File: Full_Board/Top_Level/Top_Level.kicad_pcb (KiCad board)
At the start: 2 copper layers, 160 parts, among them IC1 DRV8824QPWPRQ1, IC2 DRV8824QPWPRQ1, IC3 DRV8824QPWPRQ1, J1 OQ0432500000G, J1-J1 Conn_01x10, J1/J3 SSQ-110-03-T-D, J10 TSW-149-07-S-D, J101 PEC10DAAN, J108 TC2050-IDC-NL-FP, J12 PEC03SAAN, J13 PEC03SAAN, J2 OQ0432500000G, J2/J4 SSQ-110-03-T-D, J3 OQ0432500000G, J4 OQ0212500000G, J4-J1 Conn_01x10, J5 OQ0212500000G, J5-J1 Conn_01x10, J5/J7 SSQ-110-03-T-D, J6 KLDHCX-8-0202-A, J6/J8 SSQ-110-03-T-D, J7 OQ0212500000G, J8-J1 Conn_01x10, U1 LM2576SX-3.3-NOPB, U14 1-406541-1, U7 ZX62D-AB-5P8

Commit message: Fix MSP connector spacing
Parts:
- removed BSL: AWHW-10G-0202-T, Connectors_Other.IntLib:Assman_AWHW-10G-0x02-T
- removed CE Logo: CE Mark, Logos.IntLib:CE_Mark_5mm
- removed J1-J1, J4-J1, J5-J1, J8-J1: Conn_01x10, Connector_PinSocket_2.54mm:PinSocket_2x10_P2.54mm_Vertical
- removed J1/J3, J5/J7: SSQ-110-03-T-D, Hardware.IntLib:BoosterPack_40pin_J1J3
- removed J10: TSW-149-07-S-D, Connectors_Samtec1.IntLib:Samtec_TSW-149-07-x-D
- removed J101: PEC10DAAN, Connectors_Sullins.IntLib:SULLINS_PEC10DAAN
- removed J108: TC2050-IDC-NL-FP, Connectors_Other.IntLib:Tag_TC2050-NL
- removed J12: PEC03SAAN, Connectors_Sullins.IntLib:PEC03SAAN_Launchpad_3V3
- removed J13: PEC03SAAN, Connectors_Sullins.IntLib:PEC03SAAN_Launchpad_5V0
- removed J2/J4, J6/J8: SSQ-110-03-T-D, Hardware.IntLib:BoosterPack_40pin_J2J4
- removed JP1: PEC03DAAN, Connectors_Sullins.IntLib:SULLINS_PEC03DAAN
- removed JP2, JP6, JP7: PEC02SAAN, Connectors_Sullins.IntLib:CONN_PEC02SAAN
- removed JP4, JP5: PBC02DAAN, Connectors_Sullins.IntLib:Sullins_PxC02DAAN
- removed Logo1: Texas Instruments, Logos.IntLib:TI_Stacked_Overlay_Small
- removed MH1, MH2: MTG_NoPads, Hardware.IntLib:NPTH125mil
- removed RESET_SW1, USR_SW1, USR_SW2, Wake_SW4: 1188E-1K2-V-TR, Switches.IntLib:SW_1188E
- removed TI Logo: Texas Instruments, Logos.IntLib:TI_Symbol_Overlay_Medium
- removed TI Logo 2: Texas Instruments, Logos.IntLib:TI_Horizontal_Overlay_Small
- removed the TP10 at (356.9, 160.0)
- removed the TP10 at (62.5, 174.0)
- removed the TP11 at (83.2, 155.5)
- removed the TP11 at (367.0, 157.5)
- removed the TP12 at (367.0, 127.0)
- removed the TP12 at (76.6, 160.5)
- removed the TP13 at (65.1, 169.0)
- removed the TP13 at (356.9, 127.0)
- removed the TP14 at (78.2, 155.5)
- removed the TP14 at (384.8, 167.6)
- removed the TP15 at (117.0, 138.8)
- removed the TP15 at (336.6, 106.7)
- removed the TP16 at (361.9, 94.0)
- removed the TP16 at (116.4, 143.9)
- removed the TP17 at (372.1, 108.0)
- removed the TP17 at (108.8, 148.1)
- removed the TP4 at (75.2, 120.7)
- removed the TP4 at (364.5, 177.8)
- removed the TP5 at (68.6, 125.7)
- removed the TP5 at (367.0, 177.8)
- removed the TP6 at (57.1, 134.2)
- removed the TP6 at (369.6, 177.8)
- removed the TP7 at (372.1, 177.8)
- removed the TP7 at (70.2, 120.7)
- removed the TP8 at (351.8, 106.7)
- removed the TP8 at (70.7, 164.7)
- removed the TP9 at (359.4, 160.0)
- removed the TP9 at (70.1, 169.8)
- removed U14: 1-406541-1, Connectors_TE_Connectivity.IntLib:TEC_1-406541-1
- removed U7: ZX62D-AB-5P8, Connectors_Other.IntLib:Hirose-ZX62D-AB-5P8
- removed USB101: 1051640001, Connectors_Molex.IntLib:Molex_1051640001
- added D8: TPD1E10B06DPYR, TPD1E10B06DPYR:TPD1E10B06DPYR, F.Cu at (241.5, 70.6)
- added D9: TPD1E10B06DPYR, TPD1E10B06DPYR:TPD1E10B06DPYR, F.Cu at (242.3, 43.8)
- added J1-J3: Conn_01x10, Connector_PinSocket_2.54mm:PinSocket_2x10_P2.54mm_Vertical, F.Cu at (26.7, 21.6)
- added J4-J2: Conn_01x10, Connector_PinSocket_2.54mm:PinSocket_2x10_P2.54mm_Vertical, F.Cu at (69.9, 21.6)
- added J5-J7: Conn_01x10, Connector_PinSocket_2.54mm:PinSocket_2x10_P2.54mm_Vertical, F.Cu at (26.7, 85.1)
- added J8: OQ0212500000G, OQ0212500000G:OQ0212500000G, F.Cu at (231.1, 47.9)
- added J8-J6: Conn_01x10, Connector_PinSocket_2.54mm:PinSocket_2x10_P2.54mm_Vertical, F.Cu at (69.9, 85.1)
- added R43: CR0402-FX-5620GLF, CR0402-FX-5620GLF:RESC1005X40N, F.Cu at (266.9, 42.0)
- added R44: CR0402-FX-5620GLF, CR0402-FX-5620GLF:RESC1005X40N, F.Cu at (262.4, 44.9)
- added TP10: TestPoint, TestPoint:TestPoint_Keystone_5010-5014_Multipurpose, F.Cu at (128.1, 109.9)
- added TP11: TestPoint, TestPoint:TestPoint_Keystone_5010-5014_Multipurpose, F.Cu at (148.8, 91.4)
- added TP12: TestPoint, TestPoint:TestPoint_Keystone_5010-5014_Multipurpose, F.Cu at (142.2, 96.4)
- added TP13: TestPoint, TestPoint:TestPoint_Keystone_5010-5014_Multipurpose, F.Cu at (130.7, 104.9)
- added TP14: TestPoint, TestPoint:TestPoint_Keystone_5010-5014_Multipurpose, F.Cu at (143.8, 91.4)
- added TP15: TestPoint, TestPoint:TestPoint_Keystone_5010-5014_Multipurpose, F.Cu at (199.6, 29.0)
- added TP16: TestPoint, TestPoint:TestPoint_Keystone_5010-5014_Multipurpose, F.Cu at (199.1, 34.0)
- added TP17: TestPoint, TestPoint:TestPoint_Keystone_5010-5014_Multipurpose, F.Cu at (191.4, 38.3)
- added TP4: TestPoint, TestPoint:TestPoint_Keystone_5010-5014_Multipurpose, F.Cu at (196.7, 56.6)
- added TP5: TestPoint, TestPoint:TestPoint_Keystone_5010-5014_Multipurpose, F.Cu at (190.0, 61.7)
- added TP6: TestPoint, TestPoint:TestPoint_Keystone_5010-5014_Multipurpose, F.Cu at (178.5, 70.2)
- added TP7: TestPoint, TestPoint:TestPoint_Keystone_5010-5014_Multipurpose, F.Cu at (191.6, 56.6)
- added TP8: TestPoint, TestPoint:TestPoint_Keystone_5010-5014_Multipurpose, F.Cu at (136.3, 100.6)
- added TP9: TestPoint, TestPoint:TestPoint_Keystone_5010-5014_Multipurpose, F.Cu at (135.7, 105.7)
- D5: value 31DQ04 -> TPD1E10B06DPYR; footprint Diode_THT:D_DO-201AD_P15.24mm_Horizontal -> TPD1E10B06DPYR:TPD1E10B06DPYR
- D7: value TPD1E10B06DPYR -> 31DQ04; footprint TPD1E10B06DPYR:TPD1E10B06DPYR -> Diode_THT:D_DO-201AD_P15.24mm_Horizontal
- J4: value OQ0212500000G -> OQ0432500000G; footprint OQ0212500000G:OQ0212500000G -> OQ0432500000G:RHDR4W80P0X381_1X4_1540X700X920P
- J6: value KLDHCX-8-0202-A -> OQ0212500000G; footprint KLDHCX-8-0202-A:KLDHCX80202A -> OQ0212500000G:OQ0212500000G
- J7: value OQ0212500000G -> KLDHCX-8-0202-A; footprint OQ0212500000G:OQ0212500000G -> KLDHCX-8-0202-A:KLDHCX80202A
- R15: value CR0402-FX-5620GLF -> 2.2 k; footprint CR0402-FX-5620GLF:RESC1005X40N -> Resistor_THT:R_Axial_DIN0207_L6.3mm_D2.5mm_P10.16mm_Horizontal
- R16: value CRMA1210AF10K0DKEF -> 2.2 k; footprint CRMA1210AF10K0DKEF:RESC3225X74N -> Resistor_THT:R_Axial_DIN0207_L6.3mm_D2.5mm_P10.16mm_Horizontal
- R17, R20, R23, R26, R36, R39: value RCV2512100KFKEGAT -> CR0402-FX-5620GLF; footprint RCV2512100KFKEGAT:RESC6332X70N -> CR0402-FX-5620GLF:RESC1005X40N
- R18, R21, R24, R34, R37: value CR0402-FX-5620GLF -> CRMA1210AF10K0DKEF; footprint CR0402-FX-5620GLF:RESC1005X40N -> CRMA1210AF10K0DKEF:RESC3225X74N
- R19, R22, R25, R28, R38: value CRMA1210AF10K0DKEF -> RCV2512100KFKEGAT; footprint CRMA1210AF10K0DKEF:RESC3225X74N -> RCV2512100KFKEGAT:RESC6332X70N
- R27: value TNPV08051M00BEEA -> CRMA1210AF10K0DKEF; footprint TNPV08051M00BEEA:TNPV0805180KBEEA -> CRMA1210AF10K0DKEF:RESC3225X74N
- R29: value WSL2010R4000FEA -> TNPV08051M00BEEA; footprint WSL2010R4000FEA:RESC5025X88N -> TNPV08051M00BEEA:TNPV0805180KBEEA
- R30: value WSL2010R4000FEA -> CRMA1210AF10K0DKEF; footprint WSL2010R4000FEA:RESC5025X88N -> CRMA1210AF10K0DKEF:RESC3225X74N
- R31: value ERJ-PB6B3002V -> WSL2010R4000FEA; footprint ERJ-PB6B3002V:RESC2012X70N -> WSL2010R4000FEA:RESC5025X88N
- R32: value CRMA1210AF10K0DKEF -> WSL2010R4000FEA; footprint CRMA1210AF10K0DKEF:RESC3225X74N -> WSL2010R4000FEA:RESC5025X88N
- R33: value CRMA1210AF10K0DKEF -> ERJ-PB6B3002V; footprint CRMA1210AF10K0DKEF:RESC3225X74N -> ERJ-PB6B3002V:RESC2012X70N
- R40: value SDR10EZPJ271 -> CRMA1210AF10K0DKEF; footprint SDR10EZPJ271:RESC2012X65N -> CRMA1210AF10K0DKEF:RESC3225X74N
- R41: value CR0402-FX-5620GLF -> RCV2512100KFKEGAT; footprint CR0402-FX-5620GLF:RESC1005X40N -> RCV2512100KFKEGAT:RESC6332X70N
- R42: value CR0402-FX-5620GLF -> SDR10EZPJ271; footprint CR0402-FX-5620GLF:RESC1005X40N -> SDR10EZPJ271:RESC2012X65N
- moved D4 194.4 mm to (276.7, 19.0)
- moved J1 183.4 mm to (222.3, 22.2)
- moved J3 182.8 mm to (239.4, 30.7)
- moved R31 160.3 mm to (188.8, 19.1)
- moved C23 158.7 mm to (241.2, 47.7)
- moved R30 152.7 mm to (194.3, 28.6)
- moved TP3 152.0 mm to (176.0, 75.2)
- moved R39 151.3 mm to (237.6, 53.3)
- moved J7 150.2 mm to (161.2, 25.4)
- moved C4 145.3 mm to (184.9, 61.0)
- moved J2 143.5 mm to (239.4, 22.2)
- moved C2 143.1 mm to (173.3, 60.3)
- moved R1 143.0 mm to (179.5, 61.2)
- moved R3 142.9 mm to (173.3, 56.0)
- moved J4 141.3 mm to (222.3, 30.7)
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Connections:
- D1 pad 1: LS_Y_OUT -> /PiConnector1/Rx_MSP
- D2 pad 1: RESET_OUT -> /PiConnector1/Tx_MSP
- D3 pad 1: HOME_OUT -> LS_Y_OUT
- D4 pad 1: LS_Z_OUT -> RESET_OUT
- D5 pad 1: Net-(D5-Pad1) -> HOME_OUT
- D6 pad 1: START_OUT -> LS_Z_OUT
- D7 pad 1: LS_X_OUT -> Net-(D7-Pad1)
- J1 pad 1: /StepperDriver3/2B -> /PiConnector1/Rx_Pi
- J1 pad 2: /StepperDriver3/2A -> /PiConnector1/Tx_Pi
- J1 pad 3: /StepperDriver3/1B -> /PiConnector1/Tx_MSP
- J1 pad 4: /StepperDriver3/1A -> /PiConnector1/Rx_MSP
- J4 pad 1: GND -> /StepperDriver3/2B
- J4 pad 2: Net-(J4-Pad2) -> /StepperDriver3/2A
- J6 pad 2: +24V -> Net-(J6-Pad2)
- J7 pad 2: Net-(J7-Pad2) -> +24V
- L1 pad 2: Net-(D5-Pad1) -> Net-(D7-Pad1)
- R15 pad 1: Net-(J4-Pad2) -> /PiConnector1/Rx_MSP
- R15 pad 2: Net-(C11-Pad2) -> /PiConnector1/Tx_Pi
- R16 pad 1: Net-(C11-Pad2) -> /PiConnector1/Tx_MSP
- R16 pad 2: +3.3V -> /PiConnector1/Rx_Pi
- R17 pad 1: Net-(C11-Pad2) -> Net-(J5-Pad2)
- R17 pad 2: LS_Y_OUT -> Net-(C11-Pad2)
- R18 pad 1: Net-(R18-Pad1) -> Net-(C11-Pad2)
- R18 pad 2: Net-(C12-Pad2) -> +3.3V
- R19 pad 1: Net-(C12-Pad2) -> Net-(C11-Pad2)
- R19 pad 2: +3.3V -> LS_Y_OUT
- R20 pad 1: Net-(C12-Pad2) -> Net-(R20-Pad1)
- R20 pad 2: RESET_OUT -> Net-(C12-Pad2)
- R21 pad 1: Net-(R21-Pad1) -> Net-(C12-Pad2)
- R21 pad 2: Net-(C13-Pad2) -> +3.3V
- R22 pad 1: Net-(C13-Pad2) -> Net-(C12-Pad2)
- R22 pad 2: +3.3V -> RESET_OUT
- R23 pad 1: Net-(C13-Pad2) -> Net-(R23-Pad1)
- R23 pad 2: HOME_OUT -> Net-(C13-Pad2)
- R24 pad 1: Net-(J5-Pad2) -> Net-(C13-Pad2)
- R24 pad 2: Net-(C14-Pad2) -> +3.3V
- R25 pad 1: Net-(C14-Pad2) -> Net-(C13-Pad2)
- R25 pad 2: +3.3V -> HOME_OUT
- R26 pad 1: Net-(C14-Pad2) -> Net-(J6-Pad2)
- R26 pad 2: LS_Z_OUT -> Net-(C14-Pad2)
- R27 pad 1: +24V -> Net-(C14-Pad2)
- R27 pad 2: Net-(C18-Pad1) -> +3.3V
- R28 pad 1: GND -> Net-(C14-Pad2)
- R28 pad 2: Net-(IC3-Pad12) -> LS_Z_OUT
- R29 pad 1: GND -> +24V
- R29 pad 2: Net-(IC3-Pad6) -> Net-(C18-Pad1)
- R30 pad 2: Net-(IC3-Pad9) -> Net-(IC3-Pad12)
- R31 pad 1: Net-(C15-Pad2) -> GND
- R31 pad 2: Net-(IC3-Pad12) -> Net-(IC3-Pad6)
- R32 pad 1: Net-(C15-Pad2) -> GND
- R32 pad 2: X_FAULT -> Net-(IC3-Pad9)
- R33 pad 2: X_HOME -> Net-(IC3-Pad12)
- R34 pad 1: Net-(R34-Pad1) -> Net-(C15-Pad2)
- R34 pad 2: Net-(C22-Pad2) -> X_FAULT
- R35 pad 1: Net-(C22-Pad2) -> Net-(C15-Pad2)
- R35 pad 2: +3.3V -> X_HOME
- R36 pad 1: Net-(C22-Pad2) -> Net-(R36-Pad1)
- R36 pad 2: START_OUT -> Net-(C22-Pad2)
- R37 pad 1: Net-(J7-Pad2) -> Net-(C22-Pad2)
- R37 pad 2: Net-(C23-Pad2) -> +3.3V
- R38 pad 1: Net-(C23-Pad2) -> Net-(C22-Pad2)
- R38 pad 2: +3.3V -> START_OUT
- R39 pad 1: Net-(C23-Pad2) -> Net-(J8-Pad2)
- R39 pad 2: LS_X_OUT -> Net-(C23-Pad2)
- R40 pad 1: RED_ERROR -> Net-(C23-Pad2)
- R40 pad 2: Net-(LED1-Pad2) -> +3.3V
- R41 pad 1: Net-(LED1-Pad4) -> Net-(C23-Pad2)
- R41 pad 2: BLUE_WAIT -> LS_X_OUT
- R42 pad 1: Net-(LED1-Pad3) -> RED_ERROR
- R42 pad 2: GREEN_TAKE_TURN -> Net-(LED1-Pad2)
- S1 pad 2: Net-(R18-Pad1) -> Net-(R20-Pad1)
- S2 pad 2: Net-(R21-Pad1) -> Net-(R23-Pad1)
- S3 pad 2: Net-(R34-Pad1) -> Net-(R36-Pad1)
- U1 pad 2: Net-(D5-Pad1) -> Net-(D7-Pad1)
- U1 pad 4: Net-(D5-Pad1) -> Net-(D7-Pad1)
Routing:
- net GND: track 17.6 -> 0.00 mm
- net Y_HOME: track 14.8 -> 0.00 mm
- net XYZ_MS2: track 12.5 -> 0.00 mm

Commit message: motor1
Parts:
- moved C10 179.9 mm to (-47.5, 97.7)
- moved C6 179.9 mm to (-62.5, 109.7)
- moved C7 179.9 mm to (-54.4, 101.4)
- moved C8 179.9 mm to (-55.0, 109.0)
- moved C9 179.9 mm to (-42.7, 102.1)
- moved IC2 179.9 mm to (-62.2, 100.9)
- moved R10 179.9 mm to (-54.3, 97.1)
- moved R11 179.9 mm to (-63.2, 114.7)
- moved R12 179.9 mm to (-64.4, 118.1)
- moved R13 179.9 mm to (-57.0, 114.9)
- moved R14 179.9 mm to (-41.3, 97.3)
- moved R8 179.9 mm to (-48.1, 102.3)
- moved R9 179.9 mm to (-48.8, 106.6)
- moved TP10 179.9 mm to (-51.7, 116.3)
- moved TP11 179.9 mm to (-31.0, 97.7)
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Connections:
- J4-J2 pad 1: X_DIR -> /MSP432E401Y/PF_1
- J4-J2 pad 10: XYZ_MS1 -> XYZ_MS0
- J4-J2 pad 12: XYZ_MS2 -> X_STEP
- J4-J2 pad 14: Z_DIR -> X_ENABLE
- J4-J2 pad 16: Z_STEP -> X_DIR
- J4-J2 pad 18: Z_ENABLE -> XYZ_DECAY
- J4-J2 pad 20: Z_FAULT -> X_FAULT
- J4-J2 pad 3: X_STEP -> /MSP432E401Y/PF_2
- J4-J2 pad 4: XYZ_RESET -> X_HOME
- J4-J2 pad 5: X_ENABLE -> /MSP432E401Y/PF_3
- J4-J2 pad 6: XYZ_DECAY -> XYZ_MS2
- J4-J2 pad 7: X_HOME -> /MSP432E401Y/PG_0
- J4-J2 pad 8: XYZ_MS0 -> XYZ_MS1
- J4-J2 pad 9: X_FAULT -> /MSP432E401Y/PL_4
- J8-J6 pad 10: XYZ_MS1 -> XYZ_MS0
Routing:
- net X_FAULT: track 0.00 -> 26.9 mm
- net XYZ_DECAY: track 0.00 -> 24.4 mm
- net X_DIR: track 0.00 -> 23.2 mm
- net X_ENABLE: track 0.00 -> 20.7 mm
- net X_STEP: track 0.00 -> 19.0 mm
- net XYZ_MS0: track 0.00 -> 18.0 mm
- net XYZ_MS1: track 0.00 -> 16.3 mm
- net XYZ_MS2: track 0.00 -> 14.6 mm
- net X_HOME: track 0.00 -> 12.0 mm
- net GND: track 0.00 -> 11.2 mm

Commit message: mid layout
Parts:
- moved R2 257.1 mm to (271.4, 55.9)
- moved C6 249.6 mm to (185.4, 81.3)
- moved R13 242.7 mm to (184.0, 86.4)
- moved R7 238.7 mm to (261.6, 55.9)
- moved R12 238.3 mm to (172.7, 94.0), turned to 180 degrees
- moved R5 237.7 mm to (238.9, 92.8)
- moved C5 237.0 mm to (253.7, 55.9)
- moved TP12 236.6 mm to (198.1, 82.8)
- moved IC2 235.4 mm to (172.7, 86.4)
- moved R14 234.6 mm to (193.0, 86.4)
- moved TP14 234.3 mm to (198.1, 88.9)
- moved R1 232.8 mm to (248.6, 58.4)
- moved R4 224.0 mm to (226.1, 83.8)
- moved R11 223.6 mm to (159.3, 92.7)
- moved R6 222.4 mm to (231.1, 91.4)
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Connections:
- J1-J3 pad 10: HOME_OUT -> Z_ENABLE
- J1-J3 pad 12: BLUE_WAIT -> Z_FAULT
- J1-J3 pad 14: GREEN_TAKE_TURN -> /MSP432E401Y/PD_7
- J1-J3 pad 16: RED_ERROR -> /MSP432E401Y/PA_6
- J1-J3 pad 18: LS_X_OUT -> /MSP432E401Y/PM_4
- J1-J3 pad 20: LS_Y_OUT -> Z_HOME
- J1-J3 pad 6: START_OUT -> Z_DIR
- J1-J3 pad 8: RESET_OUT -> Z_STEP
- J5-J7 pad 11: /MSP432E401Y/PD_5 -> BLUE_WAIT
- J5-J7 pad 13: /MSP432E401Y/PQ_0 -> HOME_OUT
- J5-J7 pad 15: /MSP432E401Y/PP_4 -> RESET_OUT
- J5-J7 pad 17: /MSP432E401Y/PN_5 -> START_OUT
- J5-J7 pad 3: /MSP432E401Y/PD_2 -> LS_Y_OUT
- J5-J7 pad 5: /MSP432E401Y/PP_0 -> LS_X_OUT
- J5-J7 pad 7: /MSP432E401Y/PP_1 -> RED_ERROR
- J5-J7 pad 9: /MSP432E401Y/PD_4 -> GREEN_TAKE_TURN
- J8-J6 pad 12: /MSP432E401Y/PQ_2 -> LS_Z_OUT
- J8-J6 pad 4: Z_HOME -> XYZ_RESET
- J8-J6 pad 6: LS_Z_OUT -> /MSP432E401Y/PP_5
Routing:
- net X_FAULT: track 26.9 -> 0.00 mm
- net XYZ_DECAY: track 24.4 -> 0.00 mm
- net X_DIR: track 23.2 -> 0.00 mm
- net X_ENABLE: track 20.7 -> 0.00 mm
- net X_STEP: track 19.0 -> 0.00 mm
- net XYZ_MS0: track 18.0 -> 0.00 mm
- net XYZ_MS1: track 16.3 -> 0.00 mm
- net XYZ_MS2: track 14.6 -> 0.00 mm
- net X_HOME: track 12.0 -> 0.00 mm
- net GND: track 11.2 -> 0.63 mm

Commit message: motors placed
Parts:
- moved R2 130.8 mm to (160.0, 124.5)
- moved R7 109.7 mm to (172.7, 120.0)
- moved R1 99.6 mm to (159.7, 103.4), turned to 180 degrees
- moved R43 98.3 mm to (140.6, 115.8)
- moved C5 95.1 mm to (167.1, 95.3)
- moved R44 94.4 mm to (140.5, 120.5)
- moved LED1 93.1 mm to (140.4, 117.9)
- moved R42 91.5 mm to (144.1, 117.9)
- moved R5 79.2 mm to (166.3, 124.6)
- moved R4 73.0 mm to (160.1, 115.2)
- moved C3 70.5 mm to (160.1, 119.7)
- moved C2 70.2 mm to (159.9, 111.2)
- moved R6 67.1 mm to (172.8, 124.5)
- moved C10 54.9 mm to (172.5, 78.6)
- moved C1 53.1 mm to (172.8, 113.9)
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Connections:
- J5-J7 pad 10: /MSP432E401Y/PK_0 -> BLUE_WAIT
- J5-J7 pad 11: BLUE_WAIT -> /MSP432E401Y/PD_5
- J5-J7 pad 6: /MSP432E401Y/PB_4 -> RED_ERROR
- J5-J7 pad 7: RED_ERROR -> /MSP432E401Y/PP_1
- J5-J7 pad 8: /MSP432E401Y/PB_5 -> GREEN_TAKE_TURN
- J5-J7 pad 9: GREEN_TAKE_TURN -> /MSP432E401Y/PD_4

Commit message: switched pt1
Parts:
- moved J5 211.8 mm to (231.1, 99.1), turned to 90 degrees
- moved R16 202.6 mm to (219.0, 49.3), turned to 90 degrees
- moved D2 201.2 mm to (219.8, 53.1)
- moved D1 201.2 mm to (219.8, 56.9)
- moved R17 197.7 mm to (222.6, 95.5)
- moved R19 196.5 mm to (215.3, 97.5)
- moved R15 193.6 mm to (211.9, 56.9), turned to 90 degrees
- moved D3 192.0 mm to (222.9, 98.8)
- moved R18 190.1 mm to (207.7, 97.5), turned to 180 degrees
- moved J6 188.3 mm to (229.7, 119.6), turned to -90 degrees
- moved C11 186.3 mm to (215.9, 101.6), turned to 180 degrees
- moved R27 172.2 mm to (214.8, 116.8), turned to 180 degrees
- moved R26 168.6 mm to (216.9, 121.1), turned to 180 degrees
- moved J1 164.8 mm to (225.4, 45.5), turned to -90 degrees
- moved R28 163.7 mm to (206.9, 117.1), turned to 180 degrees
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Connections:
- J5-J7 pad 13: HOME_OUT -> /MSP432E401Y/PQ_0
- J5-J7 pad 15: RESET_OUT -> /MSP432E401Y/PP_4
- J5-J7 pad 17: START_OUT -> /MSP432E401Y/PN_5
- J5-J7 pad 3: LS_Y_OUT -> /MSP432E401Y/PD_2
- J5-J7 pad 5: LS_X_OUT -> /MSP432E401Y/PP_0
- J8-J6 pad 11: /MSP432E401Y/PM_2 -> LS_Y_OUT
- J8-J6 pad 12: LS_Z_OUT -> /MSP432E401Y/PQ_2
- J8-J6 pad 13: /MSP432E401Y/PH_0 -> LS_Z_OUT
- J8-J6 pad 3: /MSP432E401Y/PK_4 -> HOME_OUT
- J8-J6 pad 5: /MSP432E401Y/PK_5 -> RESET_OUT
- J8-J6 pad 7: /MSP432E401Y/PM_0 -> START_OUT
- J8-J6 pad 9: /MSP432E401Y/PM_1 -> LS_X_OUT

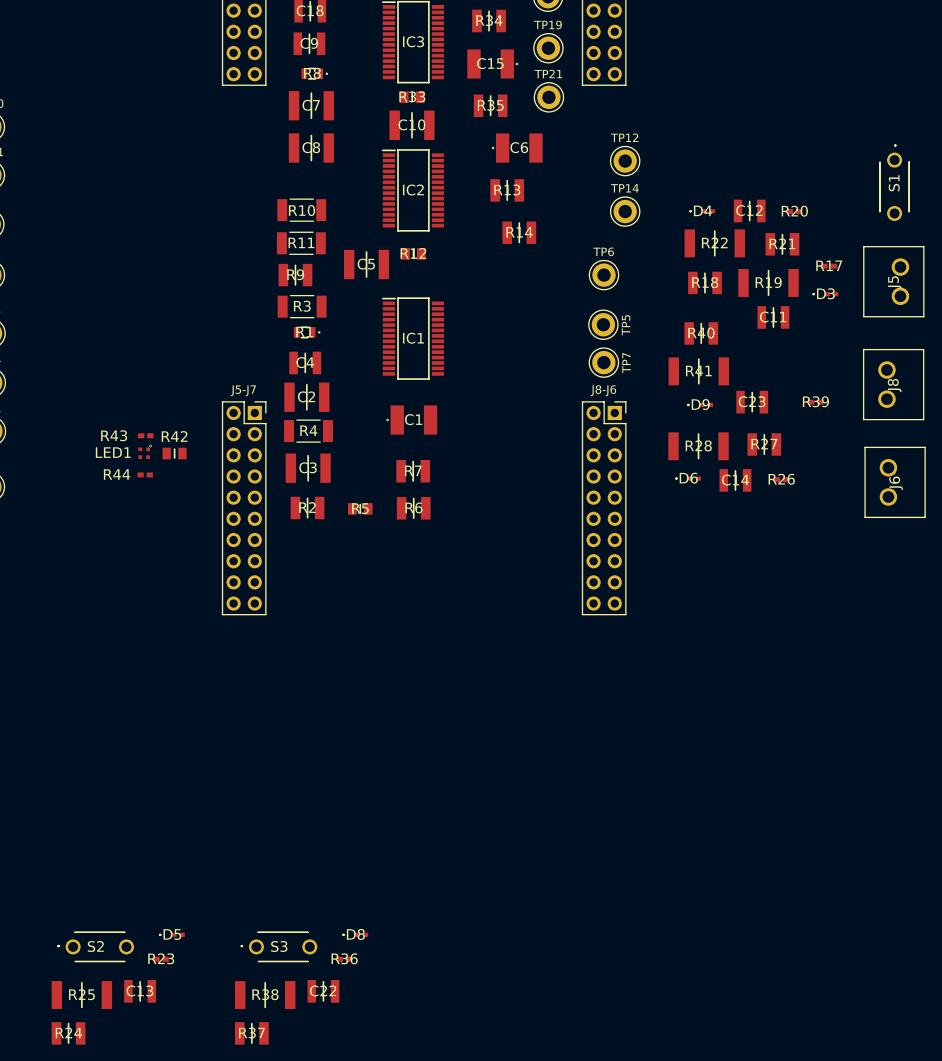
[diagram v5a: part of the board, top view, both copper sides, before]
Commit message: placed switched + buttons
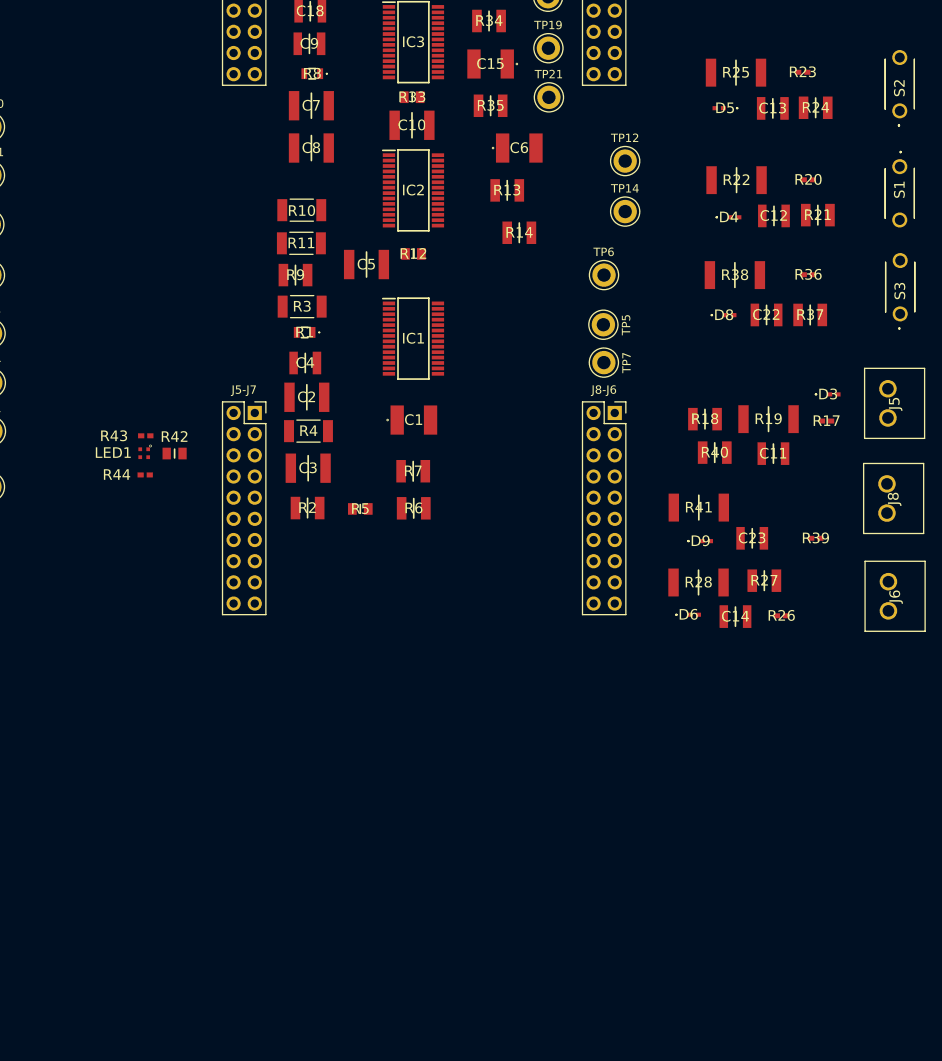
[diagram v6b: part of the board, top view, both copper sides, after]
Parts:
- moved R24 142.7 mm to (221.0, 76.4)
- moved S2 141.0 mm to (231.1, 76.8), turned to 90 degrees
- moved R25 135.6 mm to (211.4, 72.2), turned to 180 degrees
- moved R23 131.3 mm to (219.4, 72.2), turned to 180 degrees
- moved C13 130.3 mm to (215.8, 76.5)
- moved D5 118.5 mm to (209.4, 76.5), turned to 180 degrees
- moved R37 109.1 mm to (220.3, 101.3)
- moved S3 108.3 mm to (231.1, 101.2), turned to 90 degrees
- moved R38 103.1 mm to (211.3, 96.5), turned to 180 degrees
- moved R36 99.2 mm to (220.1, 96.5), turned to 180 degrees
- moved C22 97.0 mm to (215.1, 101.3)
- moved D8 86.5 mm to (210.7, 101.3)
- moved R17 18.6 mm to (222.3, 114.0)
- moved C11 16.3 mm to (215.9, 117.9)
- moved R26 16.3 mm to (216.9, 137.4)
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
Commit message: finished place
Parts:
- moved U1 129.9 mm to (159.6, 28.2)
- moved D7 114.7 mm to (137.3, 58.4), turned to 180 degrees
- moved TP23 101.2 mm to (128.2, 26.4)
- moved C20 98.5 mm to (121.0, 32.9), turned to 180 degrees
- moved L1 92.7 mm to (139.7, 48.3)
- moved TP24 86.9 mm to (118.4, 26.4)
- moved C21 81.5 mm to (127.2, 45.5), turned to 180 degrees
- moved J7 70.7 mm to (139.7, 26.1), turned to 90 degrees
- moved TP22 70.6 mm to (128.3, 33.0)
- moved TP25 46.8 mm to (123.0, 26.3)
- moved TP1 18.5 mm to (139.7, 109.9)
- moved TP8 18.5 mm to (139.5, 85.1)
- moved J3 18.5 mm to (132.7, 111.8)
- moved J4 18.5 mm to (132.7, 88.9)
- moved TP3 18.5 mm to (139.7, 98.2)
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
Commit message: tracing v1
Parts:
- moved TP17 3.68 mm to (194.8, 41.5)
- moved J2 3.67 mm to (181.5, 35.8)
- moved TP16 3.12 mm to (180.4, 41.5)
- moved TP15 1.93 mm to (185.3, 41.2)
- moved TP18 1.86 mm to (190.1, 41.4)
- turned C9 to 180 degrees
- turned R8 to 0 degrees
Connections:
- J1-J3 pad 3: /MSP432E401Y/PE_4 -> GND
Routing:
- net +24V: track 0.00 -> 112.8 mm, vias 0 -> 2
- net GND: track 0.63 -> 108.7 mm
- net Net-(D7-Pad1): track 0.00 -> 44.8 mm
- net +3.3V: track 0.00 -> 34.9 mm, vias 0 -> 2
- net Net-(C18-Pad1): track 0.00 -> 14.0 mm
- net Z_STEP: track 0.00 -> 7.17 mm
- net /StepperDriver1/1A: track 0.00 -> 6.52 mm
- net /StepperDriver1/2B: track 0.00 -> 6.16 mm
- net /StepperDriver1/1B: track 0.00 -> 5.98 mm
- net /StepperDriver1/2A: track 0.00 -> 5.47 mm
